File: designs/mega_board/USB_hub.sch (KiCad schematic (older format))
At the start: 17 parts

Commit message: Enumerate components as is in eagle design.
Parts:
- C54, C56, C60: renamed from C?; footprint (none) -> LibreRouter_MegaBoard:C0603
- C55: renamed from C?; footprint (none) -> LibreRouter_MegaBoard:UD-6,3X5,8_NICHICON
- C57, C58, C59, C61, C63: renamed from C?; footprint (none) -> LibreRouter_MegaBoard:C0402
- R81, R82, R83, R84, R85, R86: renamed from R?; footprint (none) -> LibreRouter_MegaBoard:R0402
- U12: renamed from U?; value FE1.1s -> USB_HUB_FE1.1S; footprint (none) -> LibreRouter_MegaBoard:USB_HUB_FE1.1S
- X2: renamed from Y?; footprint (none) -> LibreRouter_MegaBoard:SMARTPRJ_CRYSTAL-3.2-2.5
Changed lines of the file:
@@
 P 5950 3750
 AR Path="/5D46F2DE" Ref="U?"  Part="1"
-AR Path="/5D032896/5D46F2DE" Ref="U?"  Part="1"
-F 0 "U?" H 5950 4665 50  0000 C CNN
-F 1 "FE1.1s" H 5950 4574 50  0000 C CNN
-F 2 "" H 5950 3750 50  0001 C CNN
+AR Path="/5D032896/5D46F2DE" Ref="U12"  Part="1"
+F 0 "U12" H 5950 4665 50  0000 C CNN
+F 1 "USB_HUB_FE1.1S" H 5950 4574 50  0000 C CNN
+F 2 "LibreRouter_MegaBoard:USB_HUB_FE1.1S" H 5950 3750 50  0001 C CNN
 F 3 "" H 5950 3750 50  0001 C CNN
 	1    5950 3750
@@
 $EndComp
 $Comp
-L Device:R R?
+L Device:R R86
 U 1 1 5D46F475
 P 7650 2850
-F 0 "R?" H 7580 2804 50  0000 R CNN
+F 0 "R86" H 7580 2804 50  0000 R CNN
 F 1 "100k" H 7580 2895 50  0000 R CNN
-F 2 "" V 7580 2850 50  0001 C CNN
+F 2 "LibreRouter_MegaBoard:R0402" V 7580 2850 50  0001 C CNN
 F 3 "~" H 7650 2850 50  0001 C CNN
 	1    7650 2850
@@
 $EndComp
 $Comp
-L Device:R R?
+L Device:R R83
 U 1 1 5D46F4F0
 P 8050 2850
-F 0 "R?" H 7900 2800 50  0000 C CNN
+F 0 "R83" H 7900 2800 50  0000 C CNN
 F 1 "100k" H 7850 2900 50  0000 C CNN
-F 2 "" V 7980 2850 50  0001 C CNN
+F 2 "LibreRouter_MegaBoard:R0402" V 7980 2850 50  0001 C CNN
 F 3 "~" H 8050 2850 50  0001 C CNN
 	1    8050 2850
@@
 $EndComp
 $Comp
-L Device:R R?
+L Device:R R82
 U 1 1 5D46F542
 P 8450 2850
-F 0 "R?" H 8300 2800 50  0000 C CNN
+F 0 "R82" H 8300 2800 50  0000 C CNN
 F 1 "100k" H 8300 2900 50  0000 C CNN
-F 2 "" V 8380 2850 50  0001 C CNN
+F 2 "LibreRouter_MegaBoard:R0402" V 8380 2850 50  0001 C CNN
 F 3 "~" H 8450 2850 50  0001 C CNN
 	1    8450 2850
@@
 USB_3.3V
 $Comp
-L Device:C C?
+L Device:C C56
 U 1 1 5D46FDA8
 P 6750 4850
-F 0 "C?" H 6865 4896 50  0000 L CNN
+F 0 "C56" H 6865 4896 50  0000 L CNN
 F 1 "10uF, 10V" H 6865 4805 50  0000 L CNN
-F 2 "" H 6788 4700 50  0001 C CNN
+F 2 "LibreRouter_MegaBoard:C0603" H 6788 4700 50  0001 C CNN
 F 3 "~" H 6750 4850 50  0001 C CNN
 	1    6750 4850
@@
 $EndComp
 $Comp
-L power:GND #PWR?
+L power:GND #PWR0124
 U 1 1 5D4707A6
 P 6750 5250
-F 0 "#PWR?" H 6750 5000 50  0001 C CNN
+F 0 "#PWR0124" H 6750 5000 50  0001 C CNN
 F 1 "GND" H 6755 5077 50  0000 C CNN
 F 2 "" H 6750 5250 50  0001 C CNN
@@
 USB_3.3V
 $Comp
-L Device:C C?
+L Device:C C60
 U 1 1 5D470A72
 P 4450 4800
-F 0 "C?" H 4565 4846 50  0000 L CNN
+F 0 "C60" H 4565 4846 50  0000 L CNN
 F 1 "10uF, 10V" H 4565 4755 50  0000 L CNN
-F 2 "" H 4488 4650 50  0001 C CNN
+F 2 "LibreRouter_MegaBoard:C0603" H 4488 4650 50  0001 C CNN
 F 3 "~" H 4450 4800 50  0001 C CNN
 	1    4450 4800
@@
 	6600 4400 7100 4400
 $Comp
-L Device:R R?
+L Device:R R84
 U 1 1 5D475208
 P 9550 4350
-F 0 "R?" H 9400 4300 50  0000 C CNN
+F 0 "R84" H 9400 4300 50  0000 C CNN
 F 1 "100k" H 9350 4400 50  0000 C CNN
-F 2 "" V 9480 4350 50  0001 C CNN
+F 2 "LibreRouter_MegaBoard:R0402" V 9480 4350 50  0001 C CNN
 F 3 "~" H 9550 4350 50  0001 C CNN
 	1    9550 4350
@@
 $EndComp
 $Comp
-L Device:R R?
+L Device:R R85
 U 1 1 5D4752D0
 P 9550 3850
-F 0 "R?" H 9400 3800 50  0000 C CNN
+F 0 "R85" H 9400 3800 50  0000 C CNN
 F 1 "47k" H 9400 3900 50  0000 C CNN
-F 2 "" V 9480 3850 50  0001 C CNN
+F 2 "LibreRouter_MegaBoard:R0402" V 9480 3850 50  0001 C CNN
 F 3 "~" H 9550 3850 50  0001 C CNN
 	1    9550 3850
@@
 Connection ~ 9550 4100
 $Comp
-L Device:C C?
+L Device:C C58
 U 1 1 5D4763C3
 P 9950 4100
-F 0 "C?" H 10065 4146 50  0000 L CNN
+F 0 "C58" H 10065 4146 50  0000 L CNN
 F 1 "0.1uF" H 10065 4055 50  0000 L CNN
-F 2 "" H 9988 3950 50  0001 C CNN
+F 2 "LibreRouter_MegaBoard:C0402" H 9988 3950 50  0001 C CNN
 F 3 "~" H 9950 4100 50  0001 C CNN
 	1    9950 4100
@@
 $EndComp
 $Comp
-L Device:C C?
+L Device:C C54
 U 1 1 5D47774A
 P 7550 4850
-F 0 "C?" H 7665 4896 50  0000 L CNN
+F 0 "C54" H 7665 4896 50  0000 L CNN
 F 1 "10uF, 10V" H 7665 4805 50  0000 L CNN
-F 2 "" H 7588 4700 50  0001 C CNN
+F 2 "LibreRouter_MegaBoard:C0603" H 7588 4700 50  0001 C CNN
 F 3 "~" H 7550 4850 50  0001 C CNN
 	1    7550 4850
@@
 	1650 950  1750 950
 $Comp
-L power:GND #PWR?
+L power:GND #PWR0125
 U 1 1 5D47BDB9
 P 3700 5250
-F 0 "#PWR?" H 3700 5000 50  0001 C CNN
+F 0 "#PWR0125" H 3700 5000 50  0001 C CNN
 F 1 "GND" H 3705 5077 50  0000 C CNN
 F 2 "" H 3700 5250 50  0001 C CNN
@@
 	8200 5150 8200 5000
 $Comp
-L power:GND #PWR?
+L power:GND #PWR0126
 U 1 1 5D48386F
 P 7900 5250
-F 0 "#PWR?" H 7900 5000 50  0001 C CNN
+F 0 "#PWR0126" H 7900 5000 50  0001 C CNN
 F 1 "GND" H 7905 5077 50  0000 C CNN
 F 2 "" H 7900 5250 50  0001 C CNN
@@
 	9550 4600 9550 4500
 $Comp
-L power:GND #PWR?
+L power:GND #PWR0127
 U 1 1 5D487FAE
 P 9550 4750
-F 0 "#PWR?" H 9550 4500 50  0001 C CNN
+F 0 "#PWR0127" H 9550 4500 50  0001 C CNN
 F 1 "GND" H 9555 4577 50  0000 C CNN
 F 2 "" H 9550 4750 50  0001 C CNN
@@
 AR Path="/5D1650F5/5D48969C" Ref="C?"  Part="1"
 AR Path="/5D48969C" Ref="C?"  Part="1"
-AR Path="/5D032896/5D48969C" Ref="C?"  Part="1"
-F 0 "C?" H 8318 4896 50  0000 L CNN
+AR Path="/5D032896/5D48969C" Ref="C55"  Part="1"
+F 0 "C55" H 8318 4896 50  0000 L CNN
 F 1 "100uF, 16V" H 8318 4805 50  0000 L CNN
-F 2 "" H 8238 4700 50  0001 C CNN
+F 2 "LibreRouter_MegaBoard:UD-6,3X5,8_NICHICON" H 8238 4700 50  0001 C CNN
 F 3 "~" H 8200 4850 50  0001 C CNN
 	1    8200 4850
@@
 NoConn ~ 6950 3200
 $Comp
-L Device:C C?
+L Device:C C57
 U 1 1 5D492EC4
 P 3700 4800
-F 0 "C?" H 3815 4846 50  0000 L CNN
+F 0 "C57" H 3815 4846 50  0000 L CNN
 F 1 "0.1uF" H 3815 4755 50  0000 L CNN
-F 2 "" H 3738 4650 50  0001 C CNN
+F 2 "LibreRouter_MegaBoard:C0402" H 3738 4650 50  0001 C CNN
 F 3 "~" H 3700 4800 50  0001 C CNN
 	1    3700 4800
@@
 $EndComp
 $Comp
-L Device:C C?
+L Device:C C59
 U 1 1 5D492F4C
 P 8900 4850
-F 0 "C?" H 9015 4896 50  0000 L CNN
+F 0 "C59" H 9015 4896 50  0000 L CNN
 F 1 "0.1uF" H 9015 4805 50  0000 L CNN
-F 2 "" H 8938 4700 50  0001 C CNN
+F 2 "LibreRouter_MegaBoard:C0402" H 8938 4700 50  0001 C CNN
 F 3 "~" H 8900 4850 50  0001 C CNN
 	1    8900 4850
@@
 	8900 3100 6600 3100
 $Comp
-L power:GND #PWR?
+L power:GND #PWR0128
 U 1 1 5D4941C5
 P 8900 5200
-F 0 "#PWR?" H 8900 4950 50  0001 C CNN
+F 0 "#PWR0128" H 8900 4950 50  0001 C CNN
 F 1 "GND" H 8905 5027 50  0000 C CNN
 F 2 "" H 8900 5200 50  0001 C CNN
@@
 	8900 5000 8900 5200
 $Comp
-L power:GND #PWR?
+L power:GND #PWR0129
 U 1 1 5D49783E
 P 5200 5250
-F 0 "#PWR?" H 5200 5000 50  0001 C CNN
+F 0 "#PWR0129" H 5200 5000 50  0001 C CNN
 F 1 "GND" H 5205 5077 50  0000 C CNN
 F 2 "" H 5200 5250 50  0001 C CNN
@@
 $EndComp
 $Comp
-L Device:Crystal_GND24_Small Y?
+L Device:Crystal_GND24_Small X2
 U 1 1 5D497A3C
 P 2600 3250
-F 0 "Y?" V 3000 3250 50  0000 R CNN
+F 0 "X2" V 3000 3250 50  0000 R CNN
 F 1 "YSX321SL 12MHz" V 2900 3250 50  0000 R CNN
-F 2 "" H 2600 3250 50  0001 C CNN
+F 2 "LibreRouter_MegaBoard:SMARTPRJ_CRYSTAL-3.2-2.5" H 2600 3250 50  0001 C CNN
 F 3 "~" H 2600 3250 50  0001 C CNN
 	1    2600 3250
@@
 $EndComp
 $Comp
-L Device:C C?
+L Device:C C61
 U 1 1 5D497BD9
 P 1950 3050
-F 0 "C?" V 1698 3050 50  0000 C CNN
+F 0 "C61" V 1698 3050 50  0000 C CNN
 F 1 "18pF" V 1789 3050 50  0000 C CNN
-F 2 "" H 1988 2900 50  0001 C CNN
+F 2 "LibreRouter_MegaBoard:C0402" H 1988 2900 50  0001 C CNN
 F 3 "~" H 1950 3050 50  0001 C CNN
 	1    1950 3050
@@
 $EndComp
 $Comp
-L Device:C C?
+L Device:C C63
 U 1 1 5D497D13
 P 1950 3450
-F 0 "C?" V 1698 3450 50  0000 C CNN
+F 0 "C63" V 1698 3450 50  0000 C CNN
 F 1 "18pF" V 1789 3450 50  0000 C CNN
-F 2 "" H 1988 3300 50  0001 C CNN
+F 2 "LibreRouter_MegaBoard:C0402" H 1988 3300 50  0001 C CNN
 F 3 "~" H 1950 3450 50  0001 C CNN
 	1    1950 3450
@@
 	2350 3250 2475 3250
 $Comp
-L power:GND #PWR?
+L power:GND #PWR0130
 U 1 1 5D4B0EF8
 P 1650 3850
-F 0 "#PWR?" H 1650 3600 50  0001 C CNN
+F 0 "#PWR0130" H 1650 3600 50  0001 C CNN
 F 1 "GND" H 1655 3677 50  0000 C CNN
 F 2 "" H 1650 3850 50  0001 C CNN
@@
 	3700 4950 3700 5250
 $Comp
-L power:GND #PWR?
+L power:GND #PWR0131
 U 1 1 5D4B105C
 P 4450 5250
-F 0 "#PWR?" H 4450 5000 50  0001 C CNN
+F 0 "#PWR0131" H 4450 5000 50  0001 C CNN
 F 1 "GND" H 4455 5077 50  0000 C CNN
 F 2 "" H 4450 5250 50  0001 C CNN
@@
 $EndComp
 $Comp
-L Device:R R?
+L Device:R R81
 U 1 1 5D4B35F0
 P 5200 4800
-F 0 "R?" H 5130 4754 50  0000 R CNN
+F 0 "R81" H 5130 4754 50  0000 R CNN
 F 1 "2.7k 1%" H 5130 4845 50  0000 R CNN
-F 2 "" V 5130 4800 50  0001 C CNN
+F 2 "LibreRouter_MegaBoard:R0402" V 5130 4800 50  0001 C CNN
 F 3 "~" H 5200 4800 50  0001 C CNN
 	1    5200 4800
@@
 	5050 3100 5300 3100
 $Comp
-L power:GND #PWR?
+L power:GND #PWR0132
 U 1 1 5D4BAB00
 P 5050 5250
-F 0 "#PWR?" H 5050 5000 50  0001 C CNN
+F 0 "#PWR0132" H 5050 5000 50  0001 C CNN
 F 1 "GND" H 5055 5077 50  0000 C CNN
 F 2 "" H 5050 5250 50  0001 C CNN

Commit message: Rescue crystal module to fix new kicad miss
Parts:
- X2: symbol Device:Crystal_GND24_Small -> LibreRouter_MegaBoard-rescue:Crystal_GND24_Small-Device
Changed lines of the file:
@@
 EESchema Schematic File Version 4
 LIBS:LibreRouter_MegaBoard-cache
-EELAYER 26 0
+EELAYER 30 0
 EELAYER END
 $Descr A4 11693 8268
@@
 $EndComp
 $Comp
-L Device:Crystal_GND24_Small X2
+L LibreRouter_MegaBoard-rescue:Crystal_GND24_Small-Device X2
 U 1 1 5D497A3C
 P 2600 3250
+AR Path="/5D497A3C" Ref="X2"  Part="1"
+AR Path="/5D032896/5D497A3C" Ref="X2"  Part="1"
 F 0 "X2" V 3000 3250 50  0000 R CNN
 F 1 "YSX321SL 12MHz" V 2900 3250 50  0000 R CNN

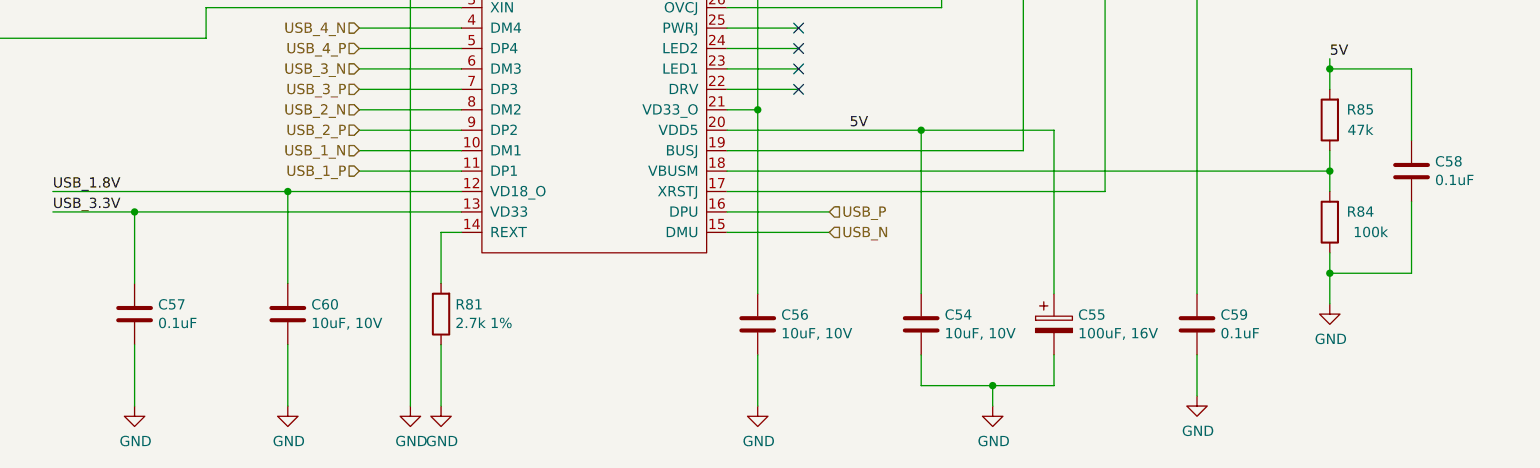
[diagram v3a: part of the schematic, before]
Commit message: Add capacitor definito to BOM
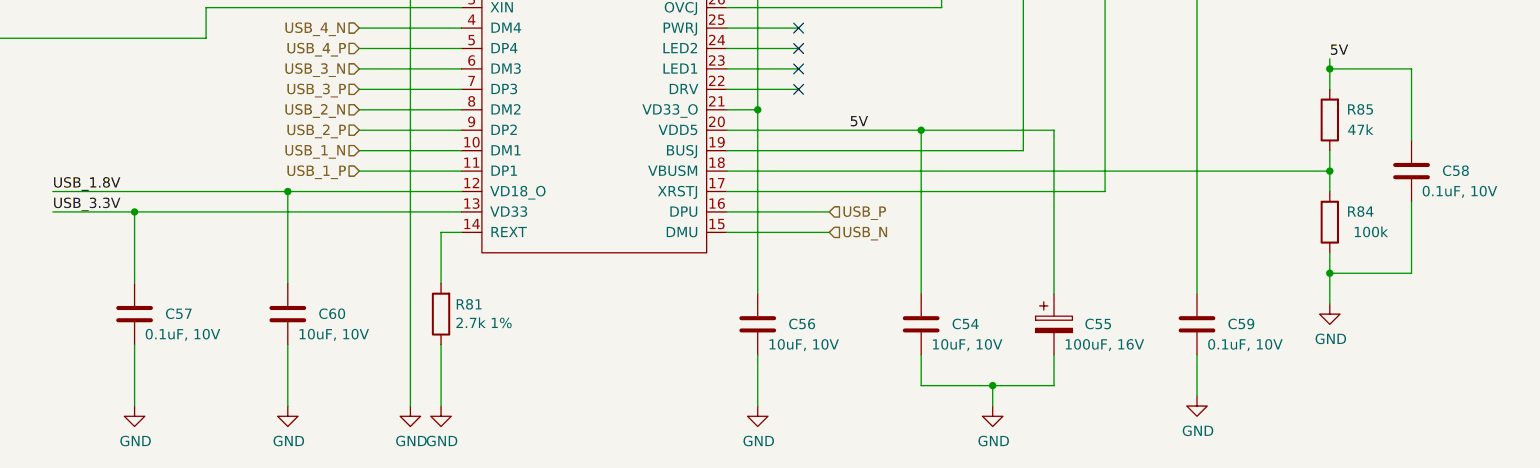
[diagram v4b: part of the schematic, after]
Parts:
- C54, C56, C60: Manufacturer (none) -> Murata Electronics; Manufacturer PN (none) -> GRM188D71A106MA73D; Supplier (none) -> DigiKey; Supplier PN (none) -> 490-7200-6-ND
- C55: Manufacturer (none) -> Nichicon; Manufacturer PN (none) -> UCL1C101MCL1GS; Supplier (none) -> DigiKey; Supplier PN (none) -> 493-3919-6-ND
- C57, C58, C59: value 0.1uF -> 0.1uF, 10V; Manufacturer (none) -> Murata Electronics; Manufacturer PN (none) -> GCM155R71A104KA55D; Supplier (none) -> DigiKey; Supplier PN (none) -> 490-16434-6-ND
- C61, C63: Manufacturer (none) -> Murata Electronics; Manufacturer PN (none) -> GCM1555C1H180JA16D; Supplier (none) -> DigiKey; Supplier PN (none) -> 490-12650-6-ND
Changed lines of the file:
@@
 U 1 1 5D46FDA8
 P 6750 4850
-F 0 "C56" H 6865 4896 50  0000 L CNN
-F 1 "10uF, 10V" H 6865 4805 50  0000 L CNN
+F 0 "C56" H 6900 4850 50  0000 L CNN
+F 1 "10uF, 10V" H 6800 4750 50  0000 L CNN
 F 2 "LibreRouter_MegaBoard:C0603" H 6788 4700 50  0001 C CNN
 F 3 "~" H 6750 4850 50  0001 C CNN
+F 4 "DigiKey" H 6750 4850 50  0001 C CNN "Supplier"
+F 5 "Murata Electronics" H 6750 4850 50  0001 C CNN "Manufacturer"
+F 6 "GRM188D71A106MA73D" H 6750 4850 50  0001 C CNN "Manufacturer PN"
+F 7 "490-7200-6-ND" H 6750 4850 50  0001 C CNN "Supplier PN"
 	1    6750 4850
 	1    0    0    -1
@@
 U 1 1 5D470A72
 P 4450 4800
-F 0 "C60" H 4565 4846 50  0000 L CNN
-F 1 "10uF, 10V" H 4565 4755 50  0000 L CNN
+F 0 "C60" H 4600 4800 50  0000 L CNN
+F 1 "10uF, 10V" H 4500 4700 50  0000 L CNN
 F 2 "LibreRouter_MegaBoard:C0603" H 4488 4650 50  0001 C CNN
 F 3 "~" H 4450 4800 50  0001 C CNN
+F 4 "DigiKey" H 4450 4800 50  0001 C CNN "Supplier"
+F 5 "Murata Electronics" H 4450 4800 50  0001 C CNN "Manufacturer"
+F 6 "GRM188D71A106MA73D" H 4450 4800 50  0001 C CNN "Manufacturer PN"
+F 7 "490-7200-6-ND" H 4450 4800 50  0001 C CNN "Supplier PN"
 	1    4450 4800
 	1    0    0    -1
@@
 U 1 1 5D4763C3
 P 9950 4100
-F 0 "C58" H 10065 4146 50  0000 L CNN
-F 1 "0.1uF" H 10065 4055 50  0000 L CNN
+F 0 "C58" H 10100 4100 50  0000 L CNN
+F 1 "0.1uF, 10V" H 10000 4000 50  0000 L CNN
 F 2 "LibreRouter_MegaBoard:C0402" H 9988 3950 50  0001 C CNN
 F 3 "~" H 9950 4100 50  0001 C CNN
+F 4 "Murata Electronics" H 9950 4100 50  0001 C CNN "Manufacturer"
+F 5 "GCM155R71A104KA55D" H 9950 4100 50  0001 C CNN "Manufacturer PN"
+F 6 "DigiKey" H 9950 4100 50  0001 C CNN "Supplier"
+F 7 "490-16434-6-ND" H 9950 4100 50  0001 C CNN "Supplier PN"
 	1    9950 4100
 	1    0    0    -1
@@
 U 1 1 5D47774A
 P 7550 4850
-F 0 "C54" H 7665 4896 50  0000 L CNN
-F 1 "10uF, 10V" H 7665 4805 50  0000 L CNN
+F 0 "C54" H 7700 4850 50  0000 L CNN
+F 1 "10uF, 10V" H 7600 4750 50  0000 L CNN
 F 2 "LibreRouter_MegaBoard:C0603" H 7588 4700 50  0001 C CNN
 F 3 "~" H 7550 4850 50  0001 C CNN
+F 4 "DigiKey" H 7550 4850 50  0001 C CNN "Supplier"
+F 5 "Murata Electronics" H 7550 4850 50  0001 C CNN "Manufacturer"
+F 6 "GRM188D71A106MA73D" H 7550 4850 50  0001 C CNN "Manufacturer PN"
+F 7 "490-7200-6-ND" H 7550 4850 50  0001 C CNN "Supplier PN"
 	1    7550 4850
 	1    0    0    -1
@@
 AR Path="/5D48969C" Ref="C?"  Part="1"
 AR Path="/5D032896/5D48969C" Ref="C55"  Part="1"
-F 0 "C55" H 8318 4896 50  0000 L CNN
-F 1 "100uF, 16V" H 8318 4805 50  0000 L CNN
+F 0 "C55" H 8350 4850 50  0000 L CNN
+F 1 "100uF, 16V" H 8250 4750 50  0000 L CNN
 F 2 "LibreRouter_MegaBoard:UD-6,3X5,8_NICHICON" H 8238 4700 50  0001 C CNN
 F 3 "~" H 8200 4850 50  0001 C CNN
+F 4 "DigiKey" H 8200 4850 50  0001 C CNN "Supplier"
+F 5 "Nichicon" H 8200 4850 50  0001 C CNN "Manufacturer"
+F 6 "UCL1C101MCL1GS" H 8200 4850 50  0001 C CNN "Manufacturer PN"
+F 7 "493-3919-6-ND" H 8200 4850 50  0001 C CNN "Supplier PN"
 	1    8200 4850
 	1    0    0    -1
@@
 U 1 1 5D492EC4
 P 3700 4800
-F 0 "C57" H 3815 4846 50  0000 L CNN
-F 1 "0.1uF" H 3815 4755 50  0000 L CNN
+F 0 "C57" H 3850 4800 50  0000 L CNN
+F 1 "0.1uF, 10V" H 3750 4700 50  0000 L CNN
 F 2 "LibreRouter_MegaBoard:C0402" H 3738 4650 50  0001 C CNN
 F 3 "~" H 3700 4800 50  0001 C CNN
+F 4 "Murata Electronics" H 3700 4800 50  0001 C CNN "Manufacturer"
+F 5 "GCM155R71A104KA55D" H 3700 4800 50  0001 C CNN "Manufacturer PN"
+F 6 "DigiKey" H 3700 4800 50  0001 C CNN "Supplier"
+F 7 "490-16434-6-ND" H 3700 4800 50  0001 C CNN "Supplier PN"
 	1    3700 4800
 	1    0    0    -1
@@
 U 1 1 5D492F4C
 P 8900 4850
-F 0 "C59" H 9015 4896 50  0000 L CNN
-F 1 "0.1uF" H 9015 4805 50  0000 L CNN
+F 0 "C59" H 9050 4850 50  0000 L CNN
+F 1 "0.1uF, 10V" H 8950 4750 50  0000 L CNN
 F 2 "LibreRouter_MegaBoard:C0402" H 8938 4700 50  0001 C CNN
 F 3 "~" H 8900 4850 50  0001 C CNN
+F 4 "Murata Electronics" H 8900 4850 50  0001 C CNN "Manufacturer"
+F 5 "GCM155R71A104KA55D" H 8900 4850 50  0001 C CNN "Manufacturer PN"
+F 6 "DigiKey" H 8900 4850 50  0001 C CNN "Supplier"
+F 7 "490-16434-6-ND" H 8900 4850 50  0001 C CNN "Supplier PN"
 	1    8900 4850
 	1    0    0    -1
@@
 F 2 "LibreRouter_MegaBoard:C0402" H 1988 2900 50  0001 C CNN
 F 3 "~" H 1950 3050 50  0001 C CNN
+F 4 "DigiKey" H 1950 3050 50  0001 C CNN "Supplier"
+F 5 "Murata Electronics" H 1950 3050 50  0001 C CNN "Manufacturer"
+F 6 "GCM1555C1H180JA16D" H 1950 3050 50  0001 C CNN "Manufacturer PN"
+F 7 "490-12650-6-ND" H 1950 3050 50  0001 C CNN "Supplier PN"
 	1    1950 3050
-	0    1    1    0
-$EndComp
-$Comp
-L Device:C C63
-U 1 1 5D497D13
-P 1950 3450
-F 0 "C63" V 1698 3450 50  0000 C CNN
-F 1 "18pF" V 1789 3450 50  0000 C CNN
-F 2 "LibreRouter_MegaBoard:C0402" H 1988 3300 50  0001 C CNN
-F 3 "~" H 1950 3450 50  0001 C CNN
-	1    1950 3450
 	0    1    1    0
 $EndComp
@@
 	1    0    0    -1
 $EndComp
+$Comp
+L Device:C C63
+U 1 1 5D497D13
+P 1950 3450
+F 0 "C63" V 1698 3450 50  0000 C CNN
+F 1 "18pF" V 1789 3450 50  0000 C CNN
+F 2 "LibreRouter_MegaBoard:C0402" H 1988 3300 50  0001 C CNN
+F 3 "~" H 1950 3450 50  0001 C CNN
+F 4 "DigiKey" H 1950 3450 50  0001 C CNN "Supplier"
+F 5 "Murata Electronics" H 1950 3450 50  0001 C CNN "Manufacturer"
+F 6 "GCM1555C1H180JA16D" H 1950 3450 50  0001 C CNN "Manufacturer PN"
+F 7 "490-12650-6-ND" H 1950 3450 50  0001 C CNN "Supplier PN"
+	1    1950 3450
+	0    1    1    0
+$EndComp
 $EndSCHEMATC
